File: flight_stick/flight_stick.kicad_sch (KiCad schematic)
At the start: 66 parts, among them J1 Load Cell 1, J10 USB_C_Receptacle_USB2.0, J11 Conn_01x05_Pin, J3 Load Cell 5, J5 Load Cell 3, J7 Conn_01x04_Male, J8 Conn_01x05_Pin, J9 Conn_ST_STDC14, Q1 MMS8550, Q3 MMS8550, Q4 2N7002, Q5 2N7002, Q6 2N7002, Q7 2N7002, Q8 2N7002, SW1 SW_Push, SW2 SW_Push, U1 HX711, U3 HX711, U4 STM32F103C8Tx, U5 LM3940IMP-3.3/NOPB, Y1 8Mhz

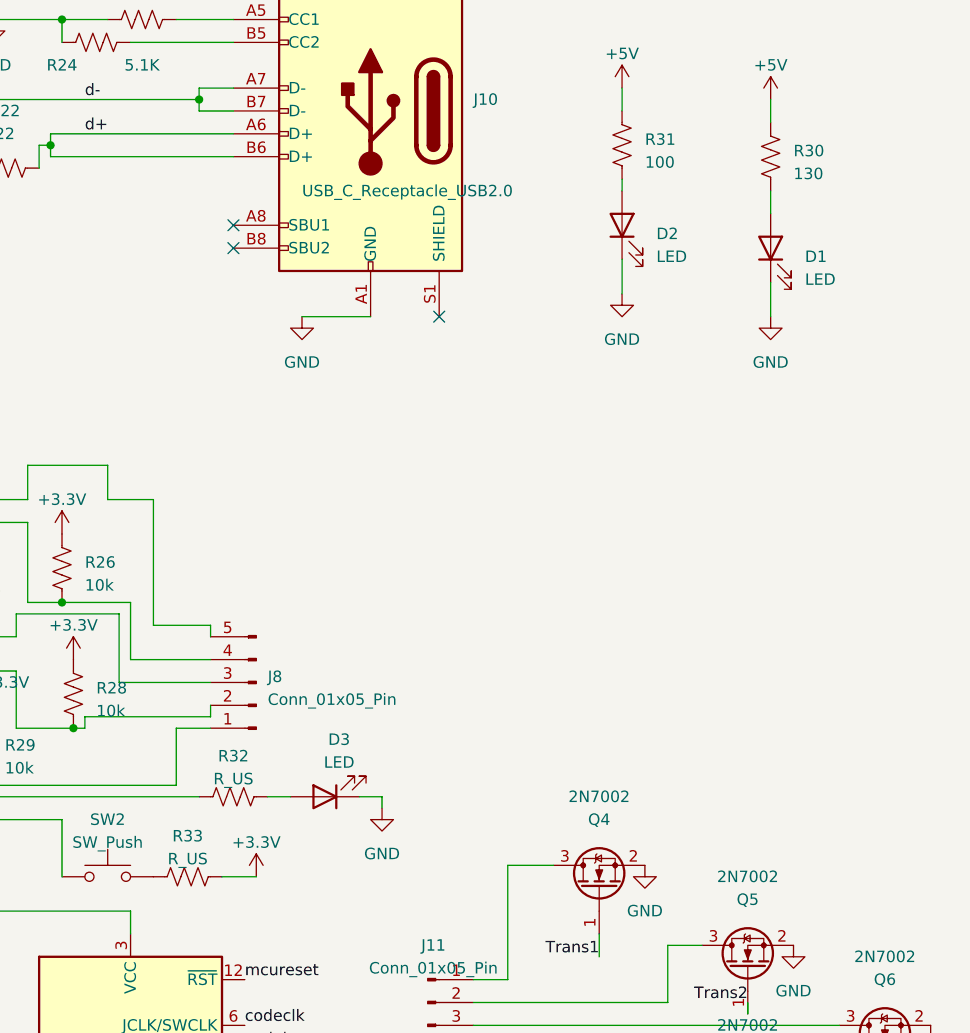
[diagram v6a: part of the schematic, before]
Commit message: Changed Resistor Values & Generated BOM
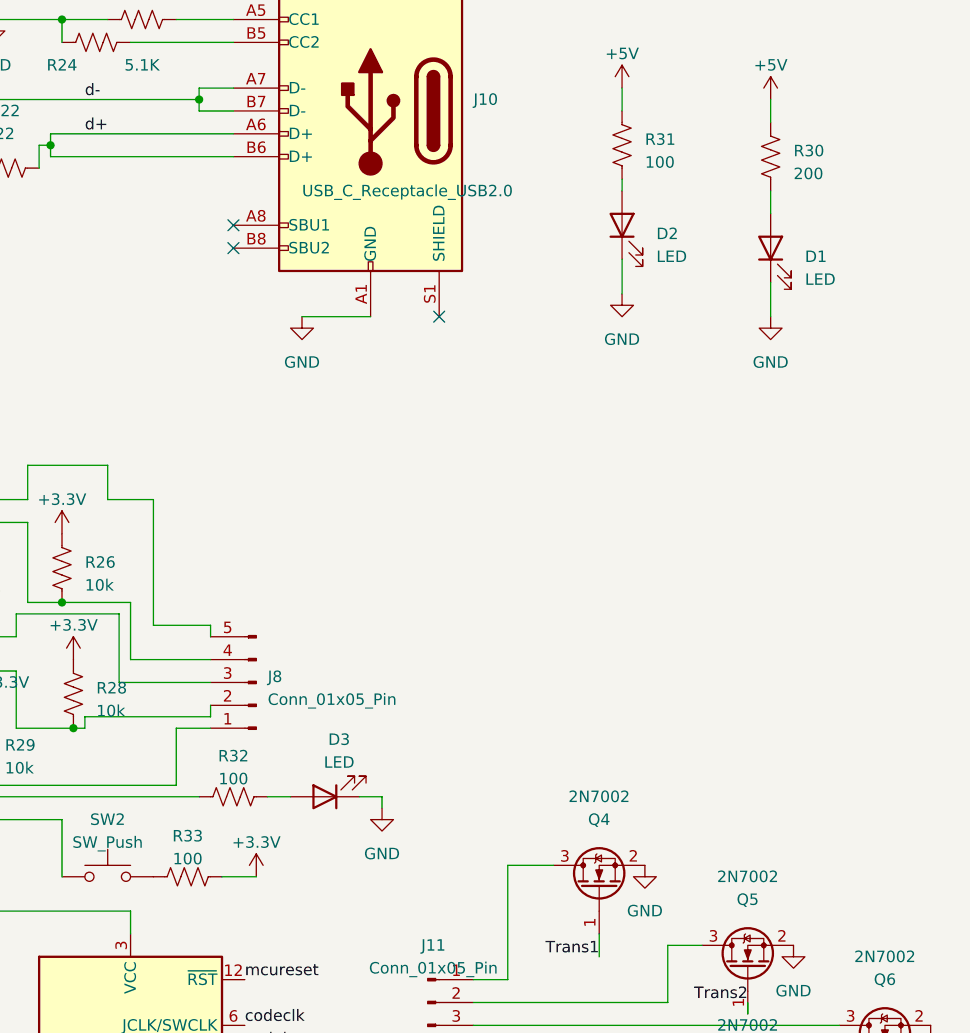
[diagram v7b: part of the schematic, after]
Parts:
- J1, J3, J5: now left out of the parts list
- R30: value 130 -> 200
- R32, R33: value R_US -> 100
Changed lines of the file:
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@@
 		(at 61.595 131.445 180)
 		(unit 1)
-		(exclude_from_sim no)
-		(in_bom yes)
+		(exclude_from_sim yes)
+		(in_bom no)
 		(on_board yes)
 		(dnp no)
@@
 			)
 		)
-		(property "Value" "R_US"
+		(property "Value" "100"
 			(at 323.85 137.7244 90)
 			(effects
@@
 			)
 		)
-		(property "Value" "R_US"
+		(property "Value" "100"
 			(at 328.93 128.8344 90)
 			(effects
@@
 		(at 57.15 50.8 180)
 		(unit 1)
-		(exclude_from_sim no)
-		(in_bom yes)
+		(exclude_from_sim yes)
+		(in_bom no)
 		(on_board yes)
 		(dnp no)
@@
 		(at 53.34 66.04 180)
 		(unit 1)
-		(exclude_from_sim no)
-		(in_bom yes)
+		(exclude_from_sim yes)
+		(in_bom no)
 		(on_board yes)
 		(dnp no)
@@
 			)
 		)
-		(property "Value" "130"
+		(property "Value" "200"
 			(at 391.16 61.595 0)
 			(effects

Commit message: Began Rev4
Changed ADC, reallocated pins, Cleaned up schematic and clear layout
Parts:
- removed C10, C14: 0.1uF, Capacitor_SMD:C_0603_1608Metric, symbol Device:C
- removed C11, C15, C7, C9: 10uF, Capacitor_SMD:C_0603_1608Metric, symbol Device:C_Polarized
- removed Q1, Q3: MMS8550, Package_TO_SOT_SMD:SOT-23, symbol Device:Q_PNP_BEC
- removed R10, R33, R9: 100, Resistor_SMD:R_0603_1608Metric, symbol Device:R_US
- removed R13, R17: 8.2k, Resistor_SMD:R_0603_1608Metric, symbol Device:R_US
- removed R14, R18: 20k, Resistor_SMD:R_0603_1608Metric, symbol Device:R_US
- removed SW2: SW_Push, Button_Switch_SMD:SW_SPST_B3U-1000P-B, symbol Switch:SW_Push
- removed U1, U3: HX711, Package_SO:SOIC-16_3.9x9.9mm_P1.27mm, symbol wing_test:HX711
- added C3: C, Capacitor_SMD:C_0603_1608Metric, symbol Device:C
- added C4: 220nF, Capacitor_SMD:C_0603_1608Metric, symbol Device:C
- added C6: 100nF, Capacitor_SMD:C_0603_1608Metric, symbol Device:C
- added R5, R6: 1k, Resistor_SMD:R_0603_1608Metric, symbol Device:R_US
- added U1: ADS131M03IRUKR, ADS131M03 Footprint:QFN_WQFN_RUK_TEX, symbol 2024-07-27_18-32-59:ADS131M03IRUKR
- C1, C2: value 0.1uF -> C
- C5: value 0.1uF -> 100nF
- D1, D2, D3: footprint LED_SMD:LED_2010_5025Metric -> LED_SMD:LED_0805_2012Metric
- J1, J5: footprint Connector_PinHeader_1.00mm:PinHeader_1x04_P1.00mm_Vertical -> Connector_PinHeader_1.27mm:PinHeader_1x04_P1.27mm_Vertical
- J3: value Load Cell 5 -> Load Cell 2; footprint Connector_PinHeader_1.00mm:PinHeader_1x04_P1.00mm_Vertical -> Connector_PinHeader_1.27mm:PinHeader_1x04_P1.27mm_Vertical
- R1, R2, R3, R4: value 100 -> 1k
- U4: value STM32F103C8Tx -> STM32F103C8T6; footprint Package_QFP:LQFP-48_7x7mm_P0.5mm -> STM32F103C8T6_UFQFPN48:QFN-48_EP_7.3x7.3_Pitch0.5mm
- U5: footprint Package_TO_SOT_SMD:SOT-223 -> LFH_Voltagereg:MP04A
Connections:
- net S-_{LC3} is gone; now on net +3.3V: J5.1 (Pin_1)
- net +3.3V: now also C5.1, J1.1 (Pin_1), J3.1 (Pin_1), R30.1, C6.1, U1.18 (DVDD), U1.19 (AVDD), U1.9 (~{RESET})
- net +5V: now also J7.1 (Pin_1); no longer J7.2 (Pin_2), R30.1
- net SCL: no longer U4.42 (PB6)
- net SDA: no longer U4.43 (PB7)
- net button1: now also J8.1 (Pin_1); no longer J8.5 (Pin_5)
- net button2: now also J8.2 (Pin_2); no longer J8.4 (Pin_4)
- net button4: now also J8.4 (Pin_4); no longer J8.2 (Pin_2)
- net button5: now also J8.5 (Pin_5); no longer J8.1 (Pin_1)
- net ADC_MCK: now reaches U4.29 (PA8)
- net ADC_MCK: now also U1.15 (CLKIN)
- net ADC_SCK: now reaches U4.39 (PB3)
- net ADC_SCK: now also U1.13 (DOUT)
- net AGND: now reaches C5.2
- net AGND: now also C16.1, C17.1, C18.1, C19.2, C20.2, C21.2, D1.1 (K), D2.1 (K), D3.1 (K), J1.4 (Pin_4), J10.A1 (GND), J10.A12 (GND), J10.B1 (GND), J10.B12 (GND), J3.4 (Pin_4), J5.4 (Pin_4), J7.2 (Pin_2), J9.11 (GNDDetect), J9.5 (GND), J9.7 (GND), Q4.2 (S), Q5.2 (S), Q6.2 (S), Q7.2 (S), Q8.2 (S), R23.1, R24.1, SW1.1, U4.23 (VSS), U4.35 (VSS), U4.44 (BOOT0), U4.47 (VSS), U4.8 (VSSA), U5.2 (GND), U5.4 (GND), Y1.2, C4.2, C6.2, U1.17 (DGND), U1.20 (AGND), U1.21 (AGND)
- net at R3.2: now also C2.2, U1.4 (AIN1P); no longer C2.1
- net at R4.2: now also C2.1, U1.3 (AIN1N); no longer C2.2
- net at R1.2: now also C1.2, U1.1 (AIN0P); no longer C1.1
- net at R2.2: now also C1.1, U1.2 (AIN0N); no longer C1.2
- net E+_{LC1&2}: no longer names the net of J1.3 (Pin_3)
- net E+_{LC1&2}: now also R2.1; no longer J3.3 (Pin_3)
- net E+_{LC3&4}: no longer names the net of J5.3 (Pin_3)
- net E+_{LC3&4}: now also R6.1
- removed net GND: C16.1, C17.1, C18.1, C19.2, C20.2, C21.2, D1.1 (K), D2.1 (K), D3.1 (K), J1.4 (Pin_4), J10.A1 (GND), J10.A12 (GND), J10.B1 (GND), J10.B12 (GND), J3.4 (Pin_4), J5.4 (Pin_4), J7.1 (Pin_1), J9.11 (GNDDetect), J9.5 (GND), J9.7 (GND), Q4.2 (S), Q5.2 (S), Q6.2 (S), Q7.2 (S), Q8.2 (S), R23.1, R24.1, SW1.1, U4.20 (PB2), U4.23 (VSS), U4.35 (VSS), U4.44 (BOOT0), U4.47 (VSS), U4.8 (VSSA), U5.2 (GND), U5.4 (GND), Y1.2
- net S+_{LC1}: no longer names the net of J1.2 (Pin_2), R1.1
- net S+_{LC2}: no longer names the net of J3.2 (Pin_2), R3.1
- net S+_{LC3}: no longer names the net of J5.2 (Pin_2)
- net S+_{LC3}: now also R5.1
- removed net S-_{LC1}: J1.1 (Pin_1), R2.1
- net S-_{LC2}: no longer names the net of R4.1
- net S-_{LC2}: now also J3.3 (Pin_3); no longer J3.1 (Pin_1)
- net clk-shear renamed ADC_SDI
- net ADC_SDI: now also U1.12 (SCLK)
- net clk-xforce: no longer names the net of U4.19 (PB1)
- net clk-yforce: no longer names the net of U4.46 (PB9)
- net dout-shear renamed ADC_SDO
- net ADC_SDO: now also U1.14 (DIN)
- net dout-xforce: no longer names the net of U4.18 (PB0)
- net dout-yforce: no longer names the net of U4.45 (PB8)
- new net: C3.2, R5.2, U1.5 (AIN2P)
- new net: C4.1, U1.16 (CAP)
- new net: C3.1, R6.2, U1.6 (AIN2N)
- new net ADC_CS: U1.10 (~{CS}), U4.42 (PB6)
- new net ADC_DRDY: U1.11 (DRDY), U4.43 (PB7)
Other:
- moved on the sheet: C16, C17, C18, C19, C20, C21, D1, D2, D3, H1, H3, J1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
